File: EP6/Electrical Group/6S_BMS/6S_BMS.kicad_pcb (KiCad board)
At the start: 4 copper layers, 213 parts, among them IC110 NX2301P,215, IC111 NX2301P,215, IC112 NX2301P,215, IC113 NX2301P,215, IC114 NX2301P,215, IC115 NX2301P,215, IC116 ADG728BRUZ, IC117 ADG728BRUZ, IC120 ADBMS1818ASWAZ-R7, IC121 AD8628ARTZ-R2, IC122 AD8628ARTZ-R2, IC201 LT8631IFE#PBF, J101 Conn_01x02, J102 Conn_01x02, J103 Conn_01x07, J104 Conn_01x16, J105 Conn_01x16, J2 CAN1, J3 Conn_01x03, J301 I_Sen, J7 I_Sen, K101 G2RL-2, Q101 2N7002, SW1 RESET, SW401 RESET, U1 TJA1051T-E, U3 STM32F103C8Tx, U6 AMS1117-3.3, U7 CAT24C256, Y1 8M

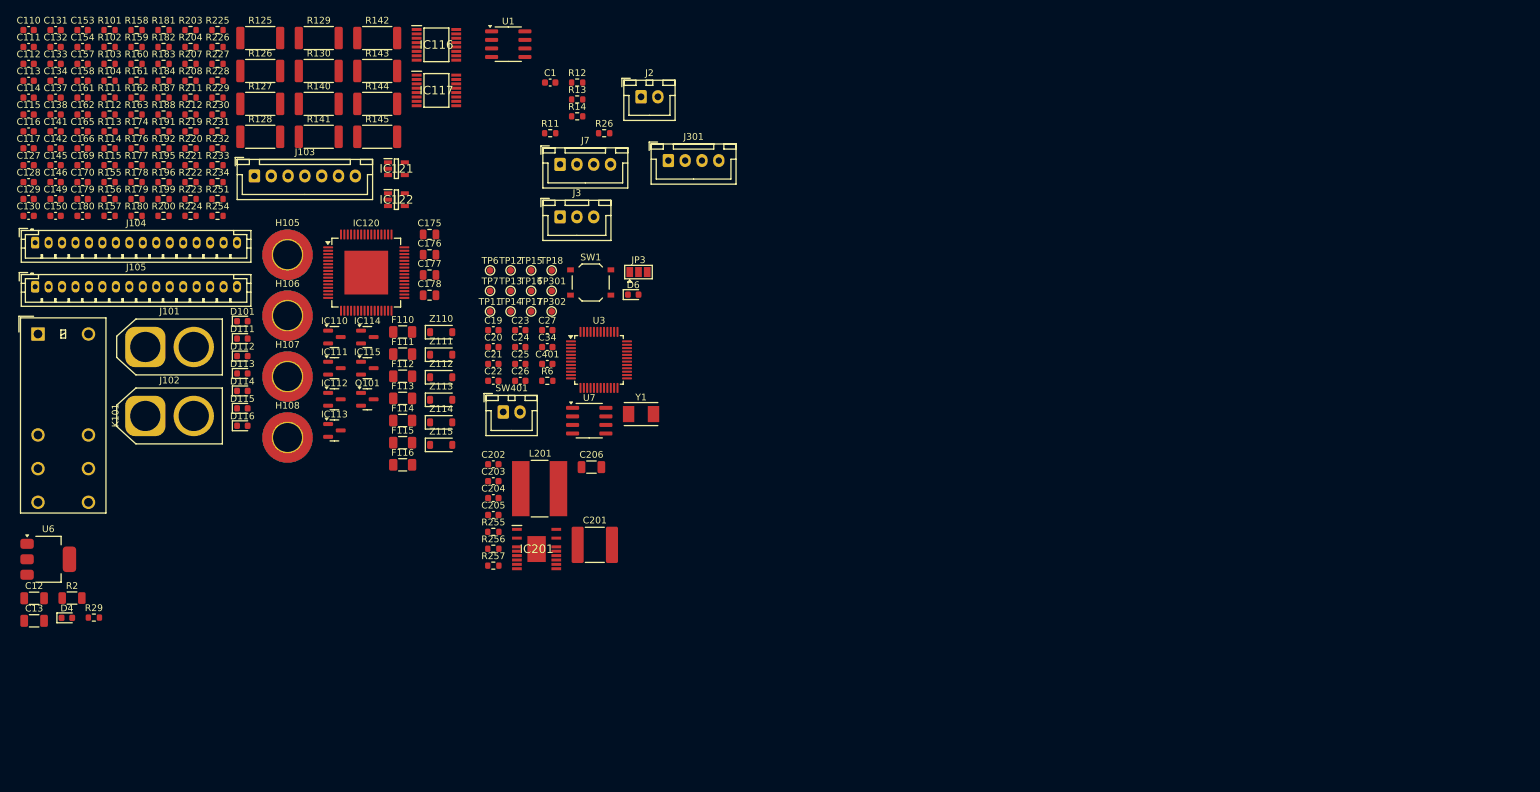
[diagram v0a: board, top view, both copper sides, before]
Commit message: update 6S_BMS  schematic and a little layout
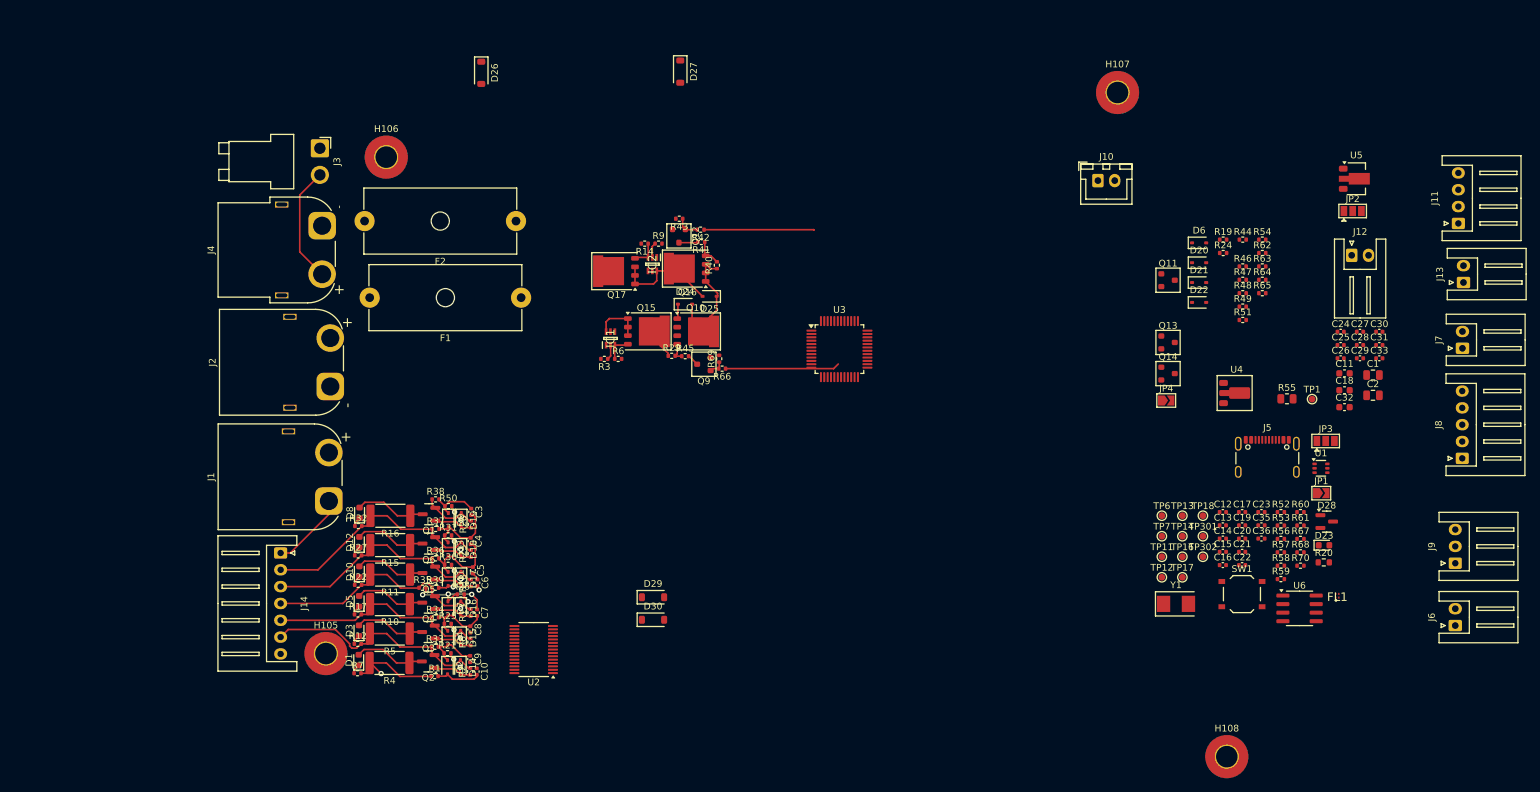
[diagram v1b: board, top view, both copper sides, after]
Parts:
- removed C110, C111, C112, C113, C114, C115, C127, C128, C129, C130, C131, C132, C137, C138, C141, C142, C145, C146, C149, C150, C153, C154, C157, C158, C161, C162, C165, C166, C169, C170: 10n, Capacitor_SMD:C_0603_1608Metric
- removed C116, C117, C133, C134: 100n, Capacitor_SMD:C_0603_1608Metric
- removed C175, C176, C177, C178: 1uF, Capacitor_SMD:C_0805_2012Metric
- removed C179, C180: 10nF, Capacitor_SMD:C_0603_1608Metric
- removed C201: 2.2u, Capacitor_SMD:C_2220_5650Metric
- removed C202: 100p, Capacitor_SMD:C_0603_1608Metric
- removed C203: 0.1u, Capacitor_SMD:C_0603_1608Metric
- removed C204: 4.7p, Capacitor_SMD:C_0603_1608Metric
- removed C205: 2.2u, Capacitor_SMD:C_0603_1608Metric
- removed C206: 22u, Capacitor_SMD:C_1206_3216Metric
- removed C34: 1u 10V, Capacitor_SMD:C_0603_1608Metric
- removed C401: 100n 16V, Capacitor_SMD:C_0603_1608Metric
- removed D101, D111, D112, D113, D114, D115, D116: RED, LED_SMD:LED_0603_1608Metric
- removed F110, F111, F112, F113, F114, F115, F116: 0466.250NR, Fuse:Fuse_1206_3216Metric
- removed IC110, IC111, IC112, IC113, IC114, IC115: NX2301P,215, Package_TO_SOT_SMD:SOT-23
- removed IC116, IC117: ADG728BRUZ, SamacSys_Parts:SOP65P640X120-16N
- removed IC120: ADBMS1818ASWAZ-R7, Package_QFP:LQFP-64-1EP_10x10mm_P0.5mm_EP6.5x6.5mm
- removed IC121, IC122: AD8628ARTZ-R2, SamacSys_Parts:SOT95P280X145-5N
- removed IC201: LT8631IFE#PBF, Samacsys:SOP65P640X120-21N
- removed J101: Conn_01x02, Connector_AMASS:AMASS_XT60-M_1x02_P7.20mm_Vertical
- removed J102: Conn_01x02, Connector_AMASS:AMASS_XT60-F_1x02_P7.20mm_Vertical
- removed J103: Conn_01x07, Connector_JST:JST_XH_B7B-XH-A_1x07_P2.50mm_Vertical
- removed J104, J105: Conn_01x16, Connector_JST:JST_PH_B16B-PH-K_1x16_P2.00mm_Vertical
- removed J301: I_Sen, Connector_JST:JST_XH_B4B-XH-A_1x04_P2.50mm_Vertical
- removed K101: G2RL-2, Relay_THT:Relay_DPDT_Omron_G2RL-2
- removed L201: 22u/2A, Inductor_SMD:L_Bourns-SRN8040_8x8.15mm
- removed Q101: 2N7002, Package_TO_SOT_SMD:SOT-23
- removed R101, R111, R112, R113, R114, R115: 510, Resistor_SMD:R_0603_1608Metric
- removed R102, R103, R183, R184, R187, R188, R191, R192, R195, R196, R199, R200, R203, R204, R207, R208, R211, R212: 10k, Resistor_SMD:R_0603_1608Metric
- removed R104, R182: 1k, Resistor_SMD:R_0603_1608Metric
- removed R125, R126, R127, R128, R129, R130, R140, R141, R142, R143, R144, R145: 130, Resistor_SMD:R_2512_6332Metric
- removed R155, R156, R157, R158, R159, R160: 3.3k, Resistor_SMD:R_0603_1608Metric
- removed R161, R162, R163, R174, R176, R177, R178, R179, R180, R181, R219, R220, R221, R222, R223, R224, R225, R226, R227, R228, R229, R230, R231, R232, R233, R234, R254: 100, Resistor_SMD:R_0603_1608Metric
- removed R251: 1M, Resistor_SMD:R_0603_1608Metric
- removed R255: 25.5k, Resistor_SMD:R_0603_1608Metric
- removed R256: 1M/1%, Resistor_SMD:R_0603_1608Metric
- removed R257: 191k/1%, Resistor_SMD:R_0603_1608Metric
- removed SW401: RESET, Connector_JST:JST_XH_B2B-XH-A_1x02_P2.50mm_Vertical
- removed TP15: CAN1_EN, TestPoint:TestPoint_Pad_D1.0mm
- removed U7: CAT24C256, Package_SO:SOIC-8_3.9x4.9mm_P1.27mm
- removed Z110, Z111, Z112, Z113, Z114, Z115: MMSZ4692T1G, Diode_SMD:D_SOD-123
- added C10: 1u, Capacitor_SMD:C_0402_1005Metric, F.Cu at (84.0, 110.9)
- added C11: 1u, Capacitor_SMD:C_0603_1608Metric, F.Cu at (213.0, 66.6)
- added C14: 10u 6V, Capacitor_SMD:C_0402_1005Metric, F.Cu at (194.9, 91.2)
- added C15: 0u1, Capacitor_SMD:C_0402_1005Metric, F.Cu at (194.9, 93.1)
- added C16: 10u 6V, Capacitor_SMD:C_0402_1005Metric, F.Cu at (194.9, 95.1)
- added C17: 10u 6V, Capacitor_SMD:C_0402_1005Metric, F.Cu at (197.8, 87.2)
- added C18: 4u7 16V, Capacitor_SMD:C_0603_1608Metric, F.Cu at (213.0, 69.1)
- added C2: 10u 25V, Capacitor_SMD:C_0805_2012Metric, F.Cu at (217.2, 69.9)
- added C28: 0u1, Capacitor_SMD:C_0402_1005Metric, F.Cu at (215.3, 62.4)
- added C29: 0u1, Capacitor_SMD:C_0402_1005Metric, F.Cu at (215.3, 64.4)
- added C3: 1u, Capacitor_SMD:C_0402_1005Metric, F.Cu at (83.2, 87.2)
- added C30: 1u, Capacitor_SMD:C_0402_1005Metric, F.Cu at (218.1, 60.4)
- added C31: 0u1, Capacitor_SMD:C_0402_1005Metric, F.Cu at (218.1, 62.4)
- added C32: 10u, Capacitor_SMD:C_0603_1608Metric, F.Cu at (213.0, 71.6)
- added C33: 10u, Capacitor_SMD:C_0402_1005Metric, F.Cu at (218.1, 64.4)
- added C35: 0u1, Capacitor_SMD:C_0402_1005Metric, F.Cu at (200.6, 89.2)
- added C36: 0u1, Capacitor_SMD:C_0402_1005Metric, F.Cu at (200.6, 91.2)
- added C4: 1u, Capacitor_SMD:C_0402_1005Metric, F.Cu at (83.1, 91.5)
- added C5: 1u, Capacitor_SMD:C_0402_1005Metric, F.Cu at (83.5, 95.9)
- added C6: 1u, Capacitor_SMD:C_0402_1005Metric, F.Cu at (84.1, 97.7)
- added C7: 1u, Capacitor_SMD:C_0402_1005Metric, F.Cu at (84.1, 102.2)
- added C8: 1u, Capacitor_SMD:C_0402_1005Metric, F.Cu at (83.1, 104.7)
- added C9: 1u, Capacitor_SMD:C_0402_1005Metric, F.Cu at (83.1, 109.1)
- added D1: RED, LED_SMD:LED_0603_1608Metric, F.Cu at (66.5, 109.2)
- added D10: RED, LED_SMD:LED_0603_1608Metric, F.Cu at (66.6, 96.1)
- added D11: BZT52C6V8S, Diode_SMD:D_SOD-323, F.Cu at (79.8, 97.2)
- added D12: RED, LED_SMD:LED_0603_1608Metric, F.Cu at (66.6, 91.7)
- added D13: BZT52C6V8S, Diode_SMD:D_SOD-323, F.Cu at (79.8, 92.8)
- added D14: BZT52C6V8S, Diode_SMD:D_SOD-323, F.Cu at (81.6, 110.3)
- added D15: BZT52C6V8S, Diode_SMD:D_SOD-323, F.Cu at (81.6, 105.9)
- added D16: BZT52C6V8S, Diode_SMD:D_SOD-323, F.Cu at (81.7, 101.5)
- added D17: BZT52C6V8S, Diode_SMD:D_SOD-323, F.Cu at (81.7, 97.2)
- added D18: BZT52C6V8S, Diode_SMD:D_SOD-323, F.Cu at (81.7, 92.8)
- added D19: BZT52C6V8S, Diode_SMD:D_SOD-323, F.Cu at (81.7, 88.4)
- added D2: BZT52C6V8S, Diode_SMD:D_SOD-323, F.Cu at (79.7, 110.3)
- added D20: 1N4148WS, Diode_SMD:D_SOD-323, F.Cu at (191.4, 50.2)
- added D21: 1N4148WS, Diode_SMD:D_SOD-323, F.Cu at (191.4, 53.1)
- added D22: BZX584C3V3, Diode_SMD:D_SOD-323, F.Cu at (191.4, 56.1)
- added D23: WHITE, LED_SMD:LED_0603_1608Metric, F.Cu at (209.9, 92.2)
- added D24: 27V, Diode_SMD:D_SOD-323, F.Cu at (115.0, 56.3)
- added D25: 27V, Diode_SMD:D_SOD-323, F.Cu at (118.6, 55.2)
- added D26: 27V, Diode_SMD:D_SOD-123, F.Cu at (84.7, 22.0)
- added D27: 27V, Diode_SMD:D_SOD-123, F.Cu at (114.3, 21.8)
- added D28: NUP2105L, Package_TO_SOT_SMD:SOT-23, F.Cu at (210.3, 88.6)
- added D29: 27V, Diode_SMD:D_SOD-123, F.Cu at (110.2, 99.9)
- added D3: RED, LED_SMD:LED_0603_1608Metric, F.Cu at (66.5, 104.9)
- added D30: 27V, Diode_SMD:D_SOD-123, F.Cu at (110.2, 103.2)
- added D5: RED, LED_SMD:LED_0603_1608Metric, F.Cu at (66.6, 100.5)
- added D7: BZT52C6V8S, Diode_SMD:D_SOD-323, F.Cu at (79.7, 101.5)
- added D8: RED, LED_SMD:LED_0603_1608Metric, F.Cu at (66.6, 87.4)
- added D9: BZT52C6V8S, Diode_SMD:D_SOD-323, F.Cu at (79.8, 88.4)
- added F1: 10A charge fuse, Fuse:Fuseholder_Cylinder-5x20mm_Schurter_0031_8201_Horizontal_Open, F.Cu at (90.6, 55.4)
- added F2: 10A discharge fuse, Fuse:Fuseholder_Cylinder-5x20mm_Schurter_0031_8201_Horizontal_Open, F.Cu at (89.9, 44.0)
- added FL1: EXC-X4CE900U, SamacSys_Parts_EP6:EXCX4CE900U, F.Cu at (211.9, 99.7)
- added IC1: DZDH0401DW-7, SamacSys_Parts_EP6:SOT65P210X110-6N, F.Cu at (103.9, 61.4)
- added IC2: DZDH0401DW-7, SamacSys_Parts_EP6:SOT65P210X110-6N, F.Cu at (110.1, 50.4)
- added J1: BATcellMain, Connector_AMASS:AMASS_XT60PW-M_1x02_P7.20mm_Horizontal, F.Cu at (62.1, 85.6)
- added J10: CAN1, Connector_JST:JST_XH_B2B-XH-A_1x02_P2.50mm_Vertical, F.Cu at (176.3, 38.0)
- added J11: frontBox, Connector_JST:JST_XH_S4B-XH-A_1x04_P2.50mm_Horizontal, F.Cu at (229.9, 44.3)
- added J12: switch, Connector_JST:JST_XH_S2B-XH-A_1x02_P2.50mm_Horizontal, F.Cu at (214.0, 49.1)
- added J13: RESET, Connector_JST:JST_XH_S2B-XH-A_1x02_P2.50mm_Horizontal, F.Cu at (230.6, 53.1)
- added J14: battery cells, Connector_JST:JST_XH_S7B-XH-A_1x07_P2.50mm_Horizontal, F.Cu at (54.9, 93.3)
- added J4: 24Vout, Connector_AMASS:AMASS_XT60PW-F_1x02_P7.20mm_Horizontal, F.Cu at (61.1, 44.7)
- added J5: USB_C_stm32, Connector_USB:USB_C_Receptacle_GCT_USB4105-xx-A_16P_TopMnt_Horizontal, F.Cu at (201.5, 80.2)
- added J6: UART2, Connector_JST:JST_XH_S2B-XH-A_1x02_P2.50mm_Horizontal, F.Cu at (229.4, 104.1)
- added J8: 7seg, Connector_JST:JST_XH_S5B-XH-A_1x05_P2.50mm_Horizontal, F.Cu at (230.5, 79.2)
- added J9: SWD, Connector_JST:JST_XH_S3B-XH-A_1x03_P2.50mm_Horizontal, F.Cu at (229.4, 94.8)
- added JP1: Vbus, Jumper:SolderJumper-2_P1.3mm_Open_TrianglePad1.0x1.5mm, F.Cu at (209.5, 84.4)
- added JP2: 3V3 source, Jumper:SolderJumper-3_P1.3mm_Open_Pad1.0x1.5mm, F.Cu at (214.2, 42.5)
- added JP4: REGSRC bypass, Jumper:SolderJumper-2_P1.3mm_Open_TrianglePad1.0x1.5mm, F.Cu at (186.5, 70.7)
- added Q1: SI2301CDS-T1-GE3, Package_TO_SOT_SMD:SOT-23, F.Cu at (76.9, 87.6)
- added Q10: HSBA3119, nturt_kicad_lib_EP6:HSBA3119_PRPAK5X6, F.Cu at (116.5, 60.4)
- added Q11: 2N7002, PCM_Package_TO_SOT_SMD_AKL:SOT-23, F.Cu at (186.7, 52.8)
- added Q12: 2N7002, PCM_Package_TO_SOT_SMD_AKL:SOT-23, F.Cu at (114.1, 46.2)
- added Q13: AO3401A, PCM_Package_TO_SOT_SMD_AKL:SOT-23, F.Cu at (186.7, 62.0)
- added Q14: 2N7002, PCM_Package_TO_SOT_SMD_AKL:SOT-23, F.Cu at (186.7, 66.7)
- added Q15: HSBA3119, nturt_kicad_lib_EP6:HSBA3119_PRPAK5X6, F.Cu at (109.2, 60.4)
- added Q16: HSBA3119, nturt_kicad_lib_EP6:HSBA3119_PRPAK5X6, F.Cu at (115.3, 51.1)
- added Q17: HSBA3119, nturt_kicad_lib_EP6:HSBA3119_PRPAK5X6, F.Cu at (104.8, 51.4)
- added Q2: SI2301CDS-T1-GE3, Package_TO_SOT_SMD:SOT-23, F.Cu at (76.8, 109.4)
- added Q3: SI2301CDS-T1-GE3, Package_TO_SOT_SMD:SOT-23, F.Cu at (76.9, 105.1)
- added Q4: SI2301CDS-T1-GE3, Package_TO_SOT_SMD:SOT-23, F.Cu at (76.9, 100.7)
- added Q5: SI2301CDS-T1-GE3, Package_TO_SOT_SMD:SOT-23, F.Cu at (76.9, 96.3)
- added Q6: SI2301CDS-T1-GE3, Package_TO_SOT_SMD:SOT-23, F.Cu at (76.9, 91.9)
- added Q9: 2N7002, PCM_Package_TO_SOT_SMD_AKL:SOT-23, F.Cu at (117.8, 65.3)
- added R1: 1k, Resistor_SMD:R_0402_1005Metric, F.Cu at (77.8, 111.6)
- added R10: 10R 2W 2512, Resistor_SMD:R_2512_6332Metric, F.Cu at (71.1, 100.9)
- added R15: 10R 2W 2512, Resistor_SMD:R_2512_6332Metric, F.Cu at (71.2, 92.1)
- added R16: 10R 2W 2512, Resistor_SMD:R_2512_6332Metric, F.Cu at (71.2, 87.8)
- added R17: 1k, Resistor_SMD:R_0402_1005Metric, F.Cu at (66.4, 102.4)
- added R18: 2M, Resistor_SMD:R_0402_1005Metric, F.Cu at (83.1, 97.8)
- added R19: 100R, Resistor_SMD:R_0402_1005Metric, F.Cu at (194.9, 46.8)
- added R20: 1k, Resistor_SMD:R_0603_1608Metric, F.Cu at (209.9, 94.7)
- added R21: 1k, Resistor_SMD:R_0402_1005Metric, F.Cu at (79.7, 108.2)
- added R22: 1k, Resistor_SMD:R_0402_1005Metric, F.Cu at (66.4, 98.0)
- added R23: 2M, Resistor_SMD:R_0402_1005Metric, F.Cu at (83.2, 93.4)
- added R24: 100R, Resistor_SMD:R_0402_1005Metric, F.Cu at (194.9, 48.7)
- added R25: 1k, Resistor_SMD:R_0402_1005Metric, F.Cu at (79.7, 103.8)
- added R27: 1k, Resistor_SMD:R_0402_1005Metric, F.Cu at (66.4, 93.7)
- added R28: 2M, Resistor_SMD:R_0402_1005Metric, F.Cu at (83.2, 89.1)
- added R3: Rref, Resistor_SMD:R_0402_1005Metric, F.Cu at (103.0, 64.5)
- added R30: 1k, Resistor_SMD:R_0402_1005Metric, F.Cu at (79.8, 95.1)
- added R31: 1k, Resistor_SMD:R_0402_1005Metric, F.Cu at (79.8, 90.7)
- added R32: 1k, Resistor_SMD:R_0402_1005Metric, F.Cu at (66.4, 89.3)
- added R33: 1k, Resistor_SMD:R_0402_1005Metric, F.Cu at (77.8, 107.2)
- added R34: 1k, Resistor_SMD:R_0402_1005Metric, F.Cu at (77.9, 102.9)
- added R35: 1k, Resistor_SMD:R_0402_1005Metric, F.Cu at (76.0, 98.5)
- added R36: 1k, Resistor_SMD:R_0402_1005Metric, F.Cu at (77.9, 94.1)
- added R37: 1k, Resistor_SMD:R_0402_1005Metric, F.Cu at (77.9, 89.7)
- added R38: 1k, Resistor_SMD:R_0402_1005Metric, F.Cu at (77.9, 85.3)
- added R39: 1k, Resistor_SMD:R_0402_1005Metric, F.Cu at (77.9, 98.5)
- added R4: 10R 2W 2512, Resistor_SMD:R_2512_6332Metric, F.Cu at (71.1, 109.7)
- added R40: 100k, Resistor_SMD:R_0402_1005Metric, F.Cu at (119.7, 50.6)
- added R41: 100k, Resistor_SMD:R_0402_1005Metric, F.Cu at (117.4, 47.1)
- added R42: 1k, Resistor_SMD:R_0402_1005Metric, F.Cu at (117.3, 45.3)
- added R43: 1M, Resistor_SMD:R_0402_1005Metric, F.Cu at (114.1, 43.6)
- added R44: 500k, Resistor_SMD:R_0402_1005Metric, F.Cu at (197.8, 46.8)
- added R45: 100k, Resistor_SMD:R_0402_1005Metric, F.Cu at (115.0, 64.1)
- added R46: 10k, Resistor_SMD:R_0402_1005Metric, F.Cu at (197.8, 50.7)
- added R47: 10k, Resistor_SMD:R_0402_1005Metric, F.Cu at (197.8, 52.7)
- added R48: 10k, Resistor_SMD:R_0402_1005Metric, F.Cu at (197.8, 54.7)
- added R49: 10k, Resistor_SMD:R_0402_1005Metric, F.Cu at (197.8, 56.7)
- added R5: 10R 2W 2512, Resistor_SMD:R_2512_6332Metric, F.Cu at (71.1, 105.3)
- added R50: 1k, Resistor_SMD:R_0402_1005Metric, F.Cu at (79.8, 86.3)
- added R51: 100R, Resistor_SMD:R_0402_1005Metric, F.Cu at (197.8, 58.7)
- added R52: 10k, Resistor_SMD:R_0402_1005Metric, F.Cu at (203.5, 87.2)
- added R53: 10k, Resistor_SMD:R_0402_1005Metric, F.Cu at (203.5, 89.2)
- added R54: 100R, Resistor_SMD:R_0402_1005Metric, F.Cu at (200.8, 46.8)
- added R55: 10R 1%, Resistor_SMD:R_0805_2012Metric, F.Cu at (204.4, 70.4)
- added R56: 10k, Resistor_SMD:R_0402_1005Metric, F.Cu at (203.5, 91.2)
- added R57: 5k1, Resistor_SMD:R_0402_1005Metric, F.Cu at (203.5, 93.2)
- added R58: 5k1, Resistor_SMD:R_0402_1005Metric, F.Cu at (203.5, 95.2)
- added R59: 10R, Resistor_SMD:R_0402_1005Metric, F.Cu at (203.5, 97.2)
- added R60: 10R, Resistor_SMD:R_0402_1005Metric, F.Cu at (206.4, 87.2)
- added R61: 1k, Resistor_SMD:R_0402_1005Metric, F.Cu at (206.4, 89.2)
- added R62: 1M, Resistor_SMD:R_0402_1005Metric, F.Cu at (200.8, 48.7)
- added R63: 1M, Resistor_SMD:R_0402_1005Metric, F.Cu at (200.8, 50.7)
- added R64: 1k, Resistor_SMD:R_0402_1005Metric, F.Cu at (200.8, 52.7)
- added R65: 1M, Resistor_SMD:R_0402_1005Metric, F.Cu at (200.8, 54.7)
- added R66: 1k, Resistor_SMD:R_0402_1005Metric, F.Cu at (120.5, 65.9)
- added R67: 100R, Resistor_SMD:R_0402_1005Metric, F.Cu at (206.4, 91.2)
- added R68: 100R, Resistor_SMD:R_0402_1005Metric, F.Cu at (206.4, 93.2)
- added R69: 1M, Resistor_SMD:R_0402_1005Metric, F.Cu at (120.1, 64.4)
- added R7: 1k, Resistor_SMD:R_0402_1005Metric, F.Cu at (66.3, 111.2)
- added R70: 10k, Resistor_SMD:R_0402_1005Metric, F.Cu at (206.4, 95.2)
- added R8: 2M, Resistor_SMD:R_0402_1005Metric, F.Cu at (83.1, 106.6)
- added R9: Rref, Resistor_SMD:R_0402_1005Metric, F.Cu at (111.0, 47.3)
- added TP1: REGOUT, TestPoint:TestPoint_Pad_D1.0mm, F.Cu at (208.1, 70.5)
- added U2: BQ7693003, Package_SO:TSSOP-30_4.4x7.8mm_P0.5mm, F.Cu at (92.5, 107.7)
- added U4: 78L05G-AB3-R, PCM_Package_TO_SOT_SMD_AKL:SOT-89-3, F.Cu at (196.6, 69.5)
- added U5: HT7533, Package_TO_SOT_SMD:SOT-89-3, F.Cu at (214.7, 37.7)
- C1: value 100n 16V -> 10u 25V; footprint Capacitor_SMD:C_0603_1608Metric -> Capacitor_SMD:C_0805_2012Metric
- C12, C13: value 10u 50V -> 30p; footprint Capacitor_SMD:C_1206_3216Metric -> Capacitor_SMD:C_0402_1005Metric
- C19: value 1u 10V -> 10u 6V; footprint Capacitor_SMD:C_0603_1608Metric -> Capacitor_SMD:C_0402_1005Metric
- C20, C21, C22, C23: value 1u 10V -> 0u1; footprint Capacitor_SMD:C_0603_1608Metric -> Capacitor_SMD:C_0402_1005Metric
- C24: value 10u 10V -> 470p; footprint Capacitor_SMD:C_0603_1608Metric -> Capacitor_SMD:C_0402_1005Metric
- C25: value 100n 16V -> 1u; footprint Capacitor_SMD:C_0603_1608Metric -> Capacitor_SMD:C_0402_1005Metric
- C26: value 15p -> 1u; footprint Capacitor_SMD:C_0603_1608Metric -> Capacitor_SMD:C_0402_1005Metric
- C27: value 15p -> 0u1; footprint Capacitor_SMD:C_0603_1608Metric -> Capacitor_SMD:C_0402_1005Metric
- D4: value 3V3Good -> BZT52C6V8S; footprint LED_SMD:LED_0603_1608Metric -> Diode_SMD:D_SOD-323
- D6: value LED -> 1N4148WS; footprint LED_SMD:LED_0603_1608Metric -> Diode_SMD:D_SOD-323
- H105, H106, H107, H108: footprint MountingHole:MountingHole_4.3mm_M4_DIN965_Pad_TopBottom -> MountingHole:MountingHole_3.2mm_M3_Pad_TopBottom
- J2: value CAN1 -> BAT charge; footprint Connector_JST:JST_XH_B2B-XH-A_1x02_P2.50mm_Vertical -> Connector_AMASS:AMASS_XT60PW-M_1x02_P7.20mm_Horizontal
- J3: value Conn_01x03 -> GLVMS; footprint Connector_JST:JST_XH_B3B-XH-A_1x03_P2.50mm_Vertical -> Connector_JST:JST_VH_B2PS-VH_1x02_P3.96mm_Horizontal
- J7: value I_Sen -> I2C1; footprint Connector_JST:JST_XH_B4B-XH-A_1x04_P2.50mm_Vertical -> Connector_JST:JST_XH_S2B-XH-A_1x02_P2.50mm_Horizontal
- R11: value 10k -> 10R 2W 2512; footprint Resistor_SMD:R_0603_1608Metric -> Resistor_SMD:R_2512_6332Metric
- R12: value 20k -> 1k; footprint Resistor_SMD:R_0603_1608Metric -> Resistor_SMD:R_0402_1005Metric
- R13: value 10k -> 2M; footprint Resistor_SMD:R_0603_1608Metric -> Resistor_SMD:R_0402_1005Metric
- R14: value 20k -> Rbias; footprint Resistor_SMD:R_0603_1608Metric -> Resistor_SMD:R_0402_1005Metric
- R2: value 1 -> 2M; footprint Resistor_SMD:R_1206_3216Metric -> Resistor_SMD:R_0402_1005Metric
- R26: value 120 -> 1k; footprint Resistor_SMD:R_0603_1608Metric -> Resistor_SMD:R_0402_1005Metric
- R29: value 2k -> 100k; footprint Resistor_SMD:R_0603_1608Metric -> Resistor_SMD:R_0402_1005Metric
- R6: value 1k -> Rbias; footprint Resistor_SMD:R_0603_1608Metric -> Resistor_SMD:R_0402_1005Metric
- U1: value TJA1051T-E -> LM66100DCK; footprint Package_SO:SOIC-8_3.9x4.9mm_P1.27mm -> Package_TO_SOT_SMD:SOT-363_SC-70-6
- U6: value AMS1117-3.3 -> TCAN1042VDRQ1; footprint Package_TO_SOT_SMD:SOT-223-3_TabPin2 -> Package_SO:SOIC-8_3.9x4.9mm_P1.27mm
- Y1: value 8M -> 8MHz X49SM8MSD2SC; footprint Crystal:Crystal_SMD_TXC_7A-2Pin_5x3.2mm -> Crystal:Crystal_SMD_5032-2Pin_5.0x3.2mm
- moved U6 186.1 mm to (206.3, 101.5)
- moved C13 177.2 mm to (194.9, 89.2)
- moved C12 177.1 mm to (194.9, 87.2)
- moved H108 147.4 mm to (195.5, 123.6)
- moved J7 136.8 mm to (230.5, 62.9), turned to 90 degrees
- moved U1 136.2 mm to (209.5, 80.7)
- moved H107 130.4 mm to (179.2, 24.9)
- moved C1 129.7 mm to (217.2, 66.9)
- moved C26 121.9 mm to (212.4, 64.4)
- moved C25 121.9 mm to (212.4, 62.4)
- moved C24 121.9 mm to (212.4, 60.4)
- moved C27 120.8 mm to (215.3, 60.4)
- moved C19 115.0 mm to (197.8, 89.2)
- moved C20 114.8 mm to (197.8, 91.2)
- moved C21 114.7 mm to (197.8, 93.1)
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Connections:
- net SPI2_CSN renamed /MCU/SPI2_CS
- net SPI2_MISO renamed /MCU/SPI2_MISO
- net SPI2_MOSI renamed /MCU/SPI2_MOSI
- net SPI2_SCK renamed /MCU/SPI2_SCK
- net UART1_RX renamed /MCU/UART1_RX
- net UART1_TX renamed /MCU/UART1_TX
- C1 pad 1: VREG -> /AFE/VC5X
- C1 pad 2: Cell0- -> /AFE/BAT
- C12 pad 1: VREG -> /MCU/OSC_IN
- C12 pad 2: Cell0- -> GND
- C13 pad 1: Net-(C13-Pad1) -> /MCU/OSC_OUT
- C13 pad 2: Cell0- -> GND
- C19 pad 1: 3V3_REF -> +3V3
- C19 pad 2: Cell0- -> GND
- C20 pad 1: 3V3_REF -> +3V3
- C20 pad 2: Cell0- -> GND
- C21 pad 1: 3V3_REF -> +3V3
- C21 pad 2: Cell0- -> GND
- C22 pad 1: 3V3_REF -> +3V3
- C22 pad 2: Cell0- -> GND
- C23 pad 1: 3V3_REF -> +3V3
- C23 pad 2: Cell0- -> GND
- C24 pad 1: 3V3_REF -> Net-(U2-ALERT)
- C24 pad 2: Cell0- -> GND
- C25 pad 1: Cell0- -> /AFE/VC5X
- C25 pad 2: SWD_RSTN -> Net-(U2-CAP2)
- C26 pad 1: Cell0- -> Net-(U2-CAP1)
- C26 pad 2: (no net) -> GND
- C27 pad 1: Cell0- -> /AFE/SRP
- C27 pad 2: (no net) -> /AFE/SRN
- D4 pad 1: Net-(D4-K) -> /AFE/C2
- D4 pad 2: 3V3_REF -> /AFE/C1
- D6 pad 1: (no net) -> /AFE/VC5X
- D6 pad 2: (no net) -> /AFE/C3
- H105 pad 1: Cell0- -> /PACK-
- H106 pad 1: Cell0- -> /PACK-
- H107 pad 1: Cell0- -> /PACK-
- H108 pad 1: Cell0- -> /PACK-
- J2 pad 1: (no net) -> /PACK-
- J2 pad 2: (no net) -> /CHARGE
- J3 pad 1: Cell0- -> /AFE/DISCHARGE
- J3 pad 2: UART2_RX -> +24V
- J7 pad 1: Cell0- -> /SCL
- J7 pad 2: (no net) -> /SDA
- JP3 pad 1: Cell0- -> GND
- JP3 pad 2: BOOT0 -> unconnected-(R61-Pad1)
- JP3 pad 3: 3V3_REF -> +3V3
- R11 pad 1: (no net) -> Net-(D10-A)
- R11 pad 2: I_Sen -> /balancing/CT3
- R12 pad 1: I_Sen -> Net-(D3-K)
- R12 pad 2: Cell0- -> /balancing/CT1
- R13 pad 1: I_Sen_Ref -> Net-(D16-A)
- R13 pad 2: (no net) -> /balancing/CT3
- R14 pad 1: I_Sen_Ref -> Net-(IC2-BIAS)
- R14 pad 2: Cell0- -> GND
- R2 pad 1: Net-(C13-Pad1) -> Net-(D14-A)
- R2 pad 2: 3V3_REF -> /balancing/CT1
- R26 pad 1: (no net) -> /AFE/C3
- R26 pad 2: (no net) -> Net-(D16-A)
- R29 pad 1: Net-(D4-K) -> /AFE/D_ideal/Vout
- R29 pad 2: Cell0- -> Net-(Q10-PadG)
- R6 pad 1: (no net) -> Net-(IC1-BIAS)
- R6 pad 2: Cell0- -> GND
- SW1 pad 1: Cell0- -> GND
- SW1 pad 2: SWD_RSTN -> /MCU/NRST
- TP14 pad 1: CAN1_S -> /MCU/CAN1_S
- TP17 pad 1: I2C1_SCL -> /SCL
- TP18 pad 1: I2C1_SDA -> /SDA
- TP301 pad 1: CAN1_RX -> /MCU/CAN1_RX
- TP302 pad 1: CAN1_TX -> /MCU/CAN1_TX
- U1 pad 1: CAN1_TX -> /MCU/VBUS
- U1 pad 2: Cell0- -> GND
- U1 pad 3: VREG -> Net-(JP1-A)
- U1 pad 4: CAN1_RX -> unconnected-(U1-NC-Pad4)
- U1 pad 5: CAN1_EN -> Net-(U1-ST)
- U1 pad 6: (no net) -> Net-(JP1-A)
- U3 pad 1: 3V3_REF -> +3V3
- U3 pad 10: I_Sen_Ref -> (no net)
- U3 pad 11: I_Sen -> (no net)
- U3 pad 12: UART2_TX -> /MCU/UART2_TX
- U3 pad 13: UART2_RX -> /MCU/UART2_RX
- U3 pad 14: OUT_EN -> (no net)
- U3 pad 15: EN_SW -> /AFE/ALERT
- U3 pad 16: (no net) -> /AFE/TS1
- U3 pad 17: (no net) -> /MCU/led
- U3 pad 21: CAN1_S -> /MCU/CAN1_S
- U3 pad 22: CAN1_EN -> (no net)
- U3 pad 23: Cell0- -> GND
- U3 pad 24: 3V3_REF -> +3V3
- U3 pad 32: (no net) -> /MCU/USB_DN
- U3 pad 33: (no net) -> /MCU/USB_DP
- U3 pad 34: SWD_SWDIO -> /MCU/SWDIO
- U3 pad 35: Cell0- -> GND
- U3 pad 36: 3V3_REF -> +3V3
- U3 pad 37: SWD_SWCLK -> /MCU/SWCLK
- U3 pad 42: I2C1_SCL -> /SCL
- U3 pad 43: I2C1_SDA -> /SDA
- U3 pad 44: BOOT0 -> /MCU/BOOT0
- U3 pad 45: CAN1_RX -> /MCU/CAN1_RX
- U3 pad 46: CAN1_TX -> /MCU/CAN1_TX
- U3 pad 47: Cell0- -> GND
- U3 pad 48: 3V3_REF -> +3V3
- U3 pad 5: (no net) -> /MCU/OSC_IN
- U3 pad 6: (no net) -> /MCU/OSC_OUT
- U3 pad 7: SWD_RSTN -> /MCU/NRST
- U3 pad 8: Cell0- -> GND
- U3 pad 9: 3V3_REF -> +3V3
- U6 pad 1: Cell0- -> Net-(U6-TXD)
- U6 pad 2: 3V3_REF -> GND
- U6 pad 3: VREG -> +5V
- Y1 pad 1: (no net) -> /MCU/OSC_IN
- Y1 pad 2: (no net) -> /MCU/OSC_OUT
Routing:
- net /balancing/CT6: track 0.00 -> 38.0 mm
- net /balancing/CT5: track 0.00 -> 35.6 mm
- net /balancing/CT1: track 0.00 -> 34.9 mm
- net /balancing/CT4: track 0.00 -> 34.8 mm
- net /balancing/CT3: track 0.00 -> 34.5 mm
- net /balancing/CT2: track 0.00 -> 33.2 mm
- net +24V: track 0.00 -> 17.4 mm
- net /AFE/D_ideal1/Vin: track 0.00 -> 17.2 mm
- net /AFE/CHG_EN: track 0.00 -> 17.0 mm
- net /AFE/DSG_EN: track 0.00 -> 16.4 mm
- net GND: track 0.00 -> 15.0 mm, vias 0 -> 1
- net /AFE/C3: track 0.00 -> 14.1 mm, vias 0 -> 3
- net /AFE/C5: track 0.00 -> 12.4 mm
- net /AFE/C4: track 0.00 -> 12.3 mm
- net Net-(D8-A): track 0.00 -> 10.6 mm
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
